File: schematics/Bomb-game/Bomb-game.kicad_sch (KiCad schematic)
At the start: 3 parts, among them U1 ADKeyboard

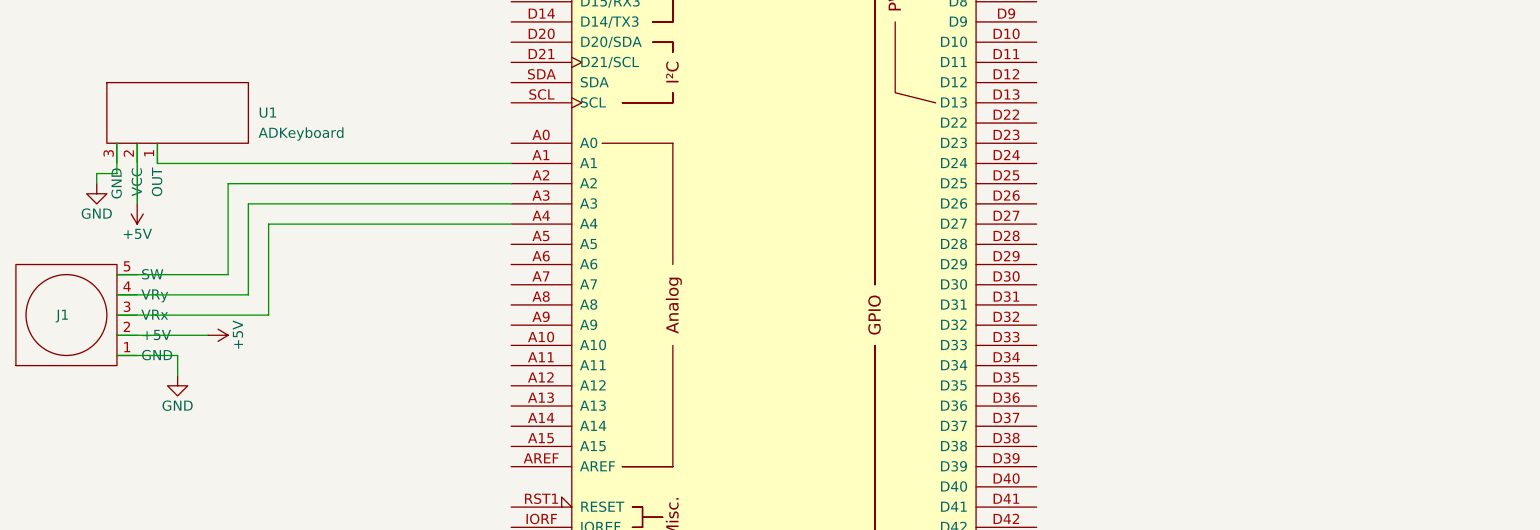
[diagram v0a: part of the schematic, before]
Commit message: Add relays to schematisc
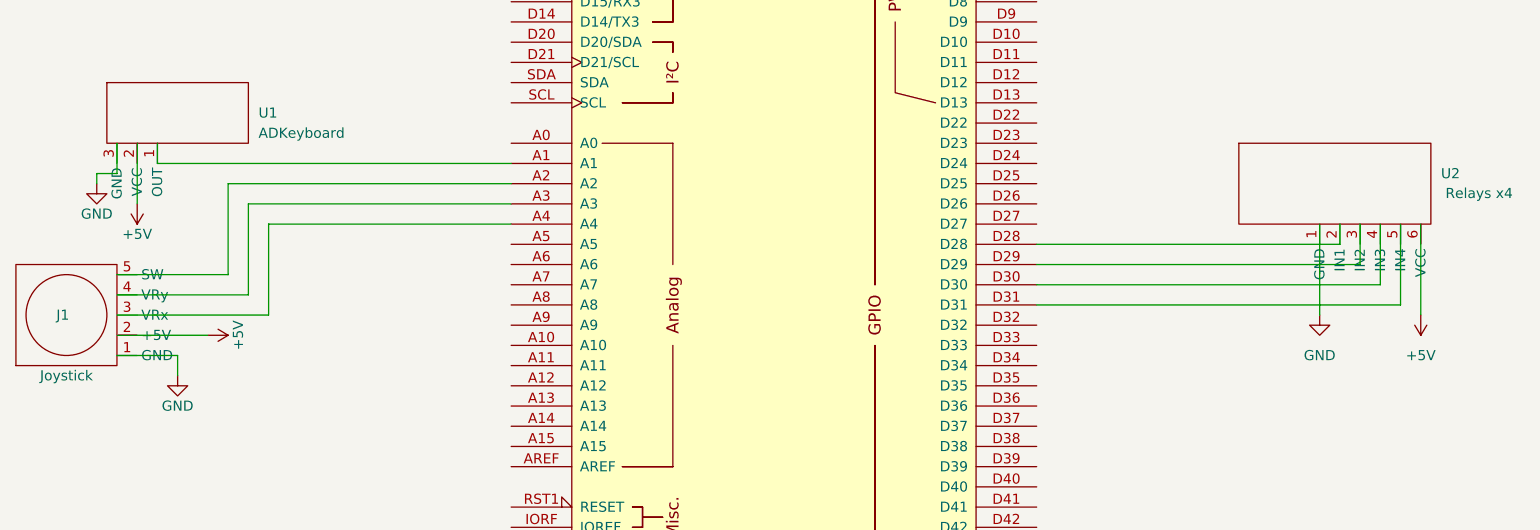
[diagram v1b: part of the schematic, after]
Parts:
- added U2: Relays x4, symbol Bomb-parts:Relay_x4
- J1: value ~ -> Joystick
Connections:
- net +5V: now also U2.6 (VCC)
- net GND: now also U2.1 (GND)
- net at XA1.D28: now also U2.2 (IN1)
- net at XA1.D29: now also U2.3 (IN2)
- net at XA1.D30: now also U2.4 (IN3)
- net at XA1.D31: now also U2.5 (IN4)
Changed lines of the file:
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@@
   (junction (at 109.22 138.43) (diameter 0) (color 0 0 0 0)
   )
+  (wire (pts (xy 220.98 72.39) (xy 220.98 82.55))
+    (stroke (width 0) (type default))
+  )
   (wire (pts (xy 73.66 78.74) (xy 73.66 67.31))
     (stroke (width 0) (type default))
@@
     (stroke (width 0) (type default))
   )
+  (wire (pts (xy 215.9 72.39) (xy 215.9 77.47))
+    (stroke (width 0) (type default))
+  )
   (wire (pts (xy 57.15 66.04) (xy 59.69 66.04))
     (stroke (width 0) (type default))
@@
     (stroke (width 0) (type default))
   )
+  (wire (pts (xy 210.82 72.39) (xy 210.82 83.82))
+    (stroke (width 0) (type default))
+  )
   (wire (pts (xy 109.22 123.19) (xy 105.41 123.19))
     (stroke (width 0) (type default))
@@
     (stroke (width 0) (type default))
   )
+  (wire (pts (xy 220.98 82.55) (xy 175.26 82.55))
+    (stroke (width 0) (type default))
+  )
   (wire (pts (xy 105.41 123.19) (xy 105.41 120.65))
     (stroke (width 0) (type default))
   )
+  (wire (pts (xy 223.52 72.39) (xy 223.52 83.82))
+    (stroke (width 0) (type default))
+  )
+  (wire (pts (xy 213.36 74.93) (xy 175.26 74.93))
+    (stroke (width 0) (type default))
+  )
   (wire (pts (xy 64.77 64.77) (xy 109.22 64.77))
     (stroke (width 0) (type default))
@@
     (stroke (width 0) (type default))
   )
+  (wire (pts (xy 215.9 77.47) (xy 175.26 77.47))
+    (stroke (width 0) (type default))
+  )
   (wire (pts (xy 105.41 118.11) (xy 109.22 118.11))
     (stroke (width 0) (type default))
@@
     (stroke (width 0) (type default))
   )
+  (wire (pts (xy 213.36 72.39) (xy 213.36 74.93))
+    (stroke (width 0) (type default))
+  )
   (wire (pts (xy 67.31 88.9) (xy 67.31 91.44))
     (stroke (width 0) (type default))
   )
+  (wire (pts (xy 218.44 80.01) (xy 175.26 80.01))
+    (stroke (width 0) (type default))
+  )
   (wire (pts (xy 59.69 86.36) (xy 71.12 86.36))
+    (stroke (width 0) (type default))
+  )
+  (wire (pts (xy 218.44 72.39) (xy 218.44 80.01))
     (stroke (width 0) (type default))
   )
@@
       (effects (font (size 1.27 1.27)) (justify right))
     )
-    (property "Value" "~" (at 55.88 86.36 0)
+    (property "Value" "Joystick" (at 53.34 91.44 90)
       (effects (font (size 1.27 1.27)))
     )
@@
         (path "/d5dfcc17-2f57-46e4-9b81-9957aca5a4a9"
           (reference "#PWR01") (unit 1)
+        )
+      )
+    )
+  )
+  (symbol (lib_id "Bomb-parts:Relay_x4") (at 214.63 68.58 0) (unit 1)
+    (in_bom yes) (on_board yes) (dnp no)
+    (property "Reference" "U2" (at 226.06 66.04 0)
+      (effects (font (size 1.27 1.27)) (justify left))
+    )
+    (property "Value" "Relays x4" (at 230.8513 68.5236 0)
+      (effects (font (size 1.27 1.27)))
+    )
+    (property "Footprint" "" (at 214.63 68.58 0)
+      (effects (font (size 1.27 1.27)) hide)
+    )
+    (property "Datasheet" "" (at 214.63 68.58 0)
+      (effects (font (size 1.27 1.27)) hide)
+    )
+    (pin "1")
+    (pin "2")
+    (pin "3")
+    (pin "4")
+    (pin "5")
+    (pin "6")
+    (instances
+      (project "Bomb-game"
+        (path "/d5dfcc17-2f57-46e4-9b81-9957aca5a4a9"
+          (reference "U2") (unit 1)
         )
       )
@@
         )
       )
+    )
+  )
+  (symbol (lib_id "power:GND") (at 210.82 83.82 0) (unit 1)
+    (in_bom yes) (on_board yes) (dnp no) (fields_autoplaced)
+    (property "Reference" "#PWR08" (at 210.82 90.17 0)
+      (effects (font (size 1.27 1.27)) hide)
+    )
+    (property "Value" "GND" (at 210.82 88.9 0)
+      (effects (font (size 1.27 1.27)))
+    )
+    (property "Footprint" "" (at 210.82 83.82 0)
+      (effects (font (size 1.27 1.27)) hide)
+    )
+    (property "Datasheet" "" (at 210.82 83.82 0)
+      (effects (font (size 1.27 1.27)) hide)
+    )
+    (pin "1")
+    (instances
+      (project "Bomb-game"
+        (path "/d5dfcc17-2f57-46e4-9b81-9957aca5a4a9"
+          (reference "#PWR08") (unit 1)
+        )
+      )
+    )
+  )
+  (symbol (lib_id "power:+5V") (at 223.52 83.82 180) (unit 1)
+    (in_bom yes) (on_board yes) (dnp no) (fields_autoplaced)
+    (property "Reference" "#PWR09" (at 223.52 80.01 0)
+      (effects (font (size 1.27 1.27)) hide)
+    )
+    (property "Value" "+5V" (at 223.52 88.9 0)
+      (effects (font (size 1.27 1.27)))
+    )
+    (property "Footprint" "" (at 223.52 83.82 0)
+      (effects (font (size 1.27 1.27)) hide)
+    )
+    (property "Datasheet" "" (at 223.52 83.82 0)
+      (effects (font (size 1.27 1.27)) hide)
+    )
+    (pin "1")
+    (instances
+      (project "Bomb-game"
+        (path "/d5dfcc17-2f57-46e4-9b81-9957aca5a4a9"
+          (reference "#PWR09") (unit 1)
+        )
+      )

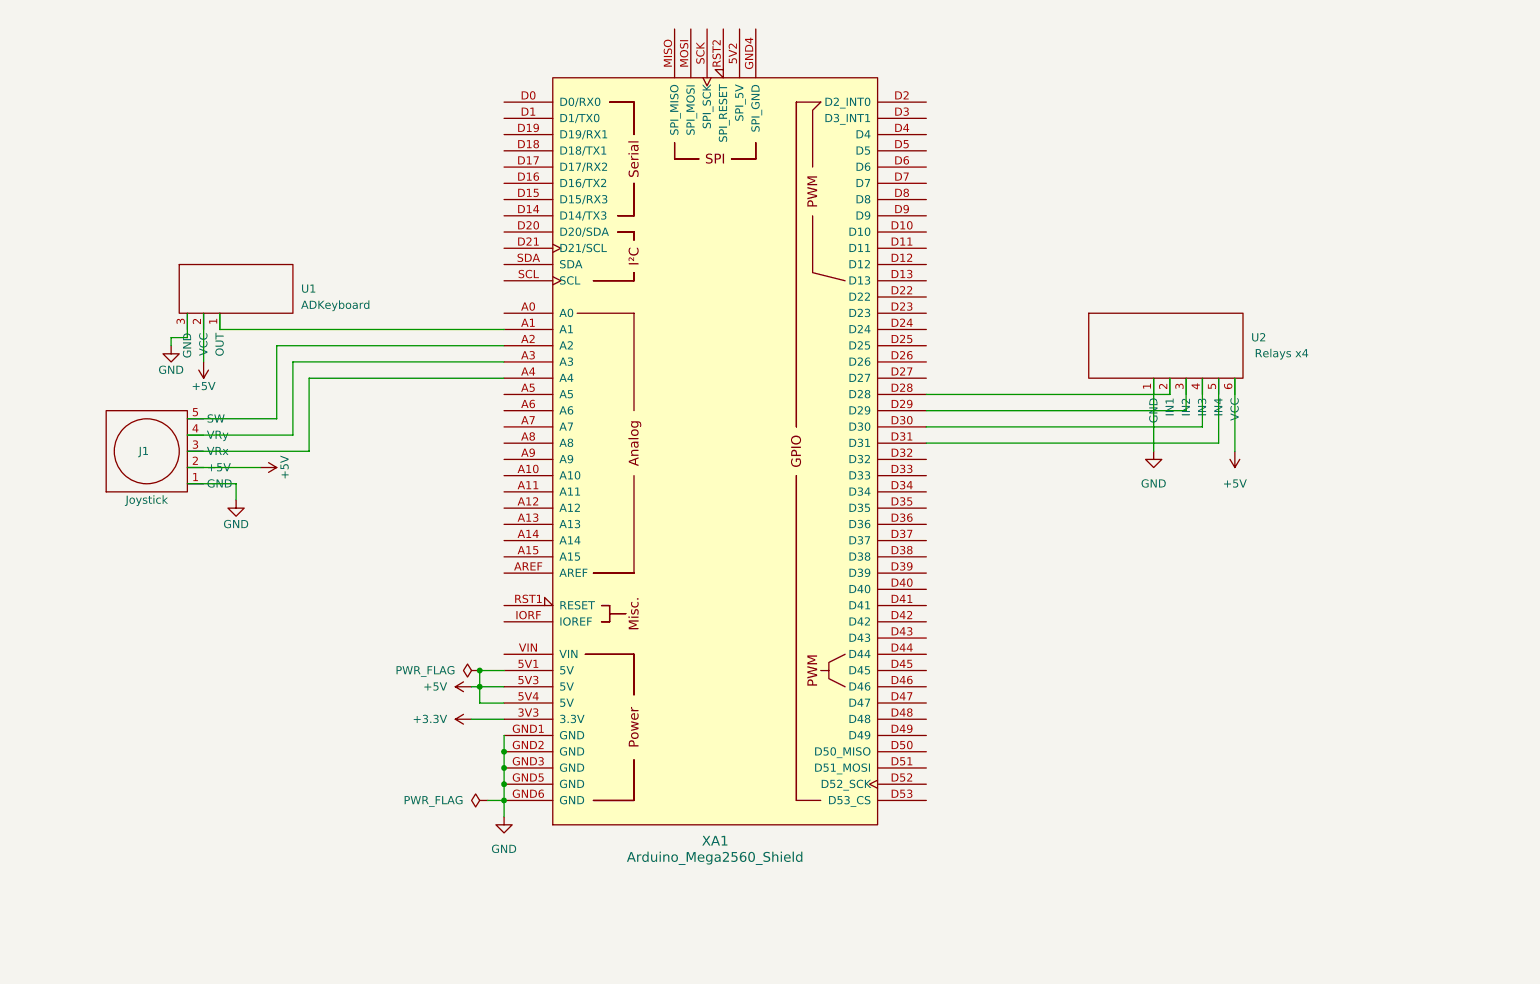
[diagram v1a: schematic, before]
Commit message: Update schematics, add emergency button
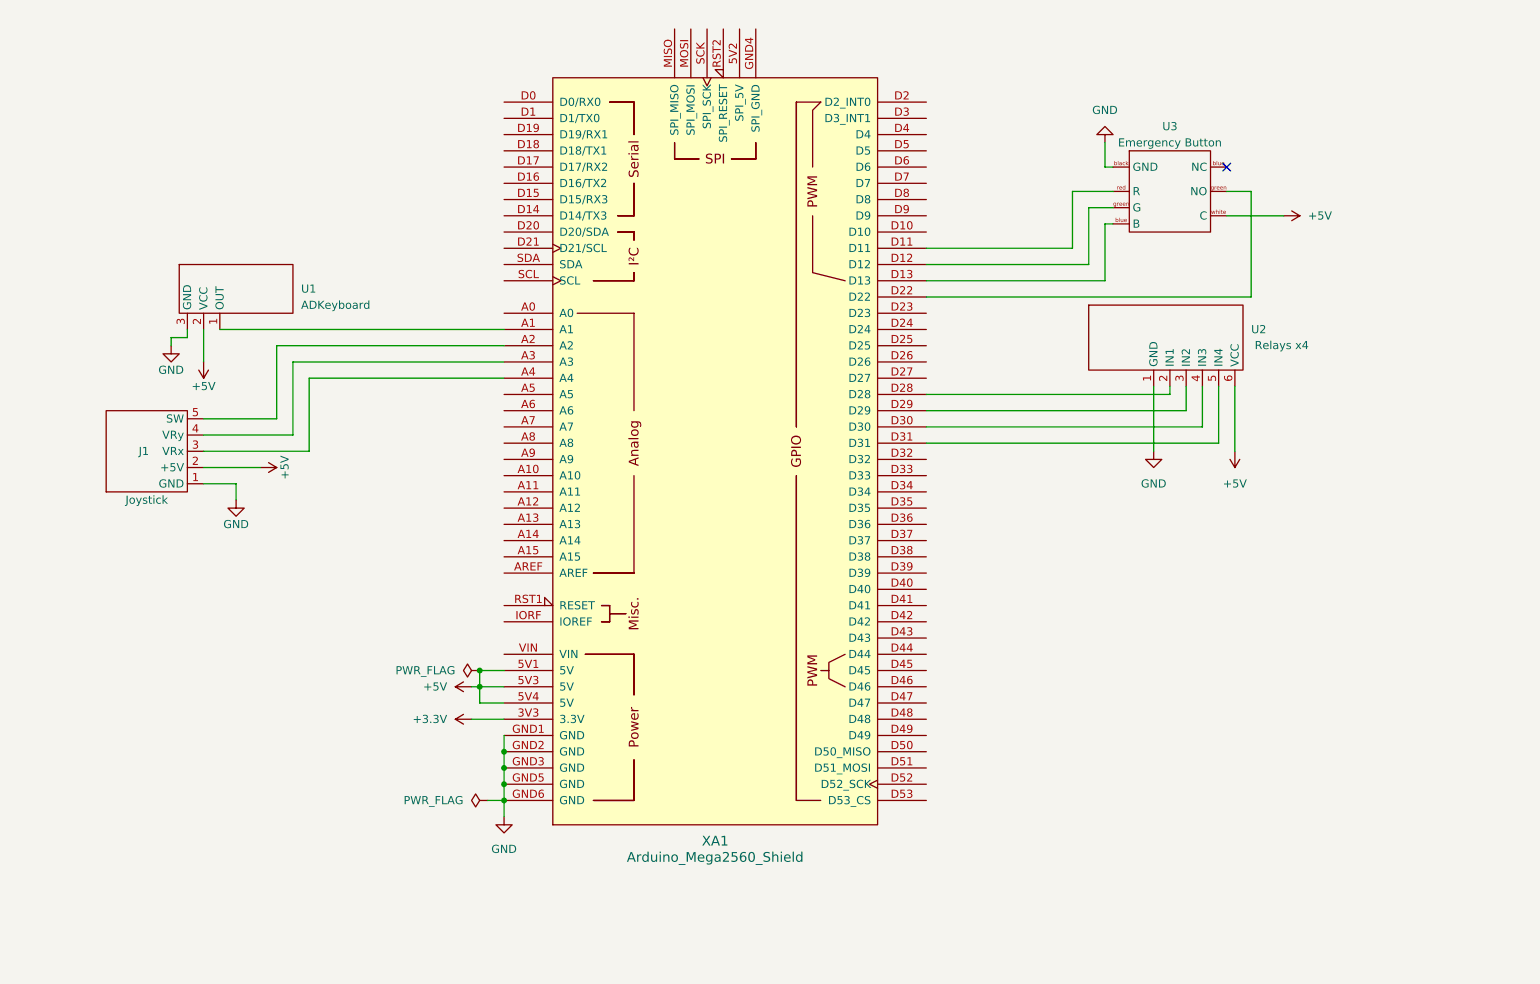
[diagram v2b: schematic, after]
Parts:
- added U3: Emergency Button, symbol Bomb-parts:Emergency_button
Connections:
- net +5V: now also U3.white (C)
- net GND: now also U3.black (GND)
- net at XA1.D11: now also U3.red (R)
- net at XA1.D12: now also U3.green (NO)
- net at XA1.D13: now also U3.blue (NC)
- net at XA1.D22: now also U3.green (NO)
- no-connect marks 0 -> 1
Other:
- moved on the sheet: U1, U2

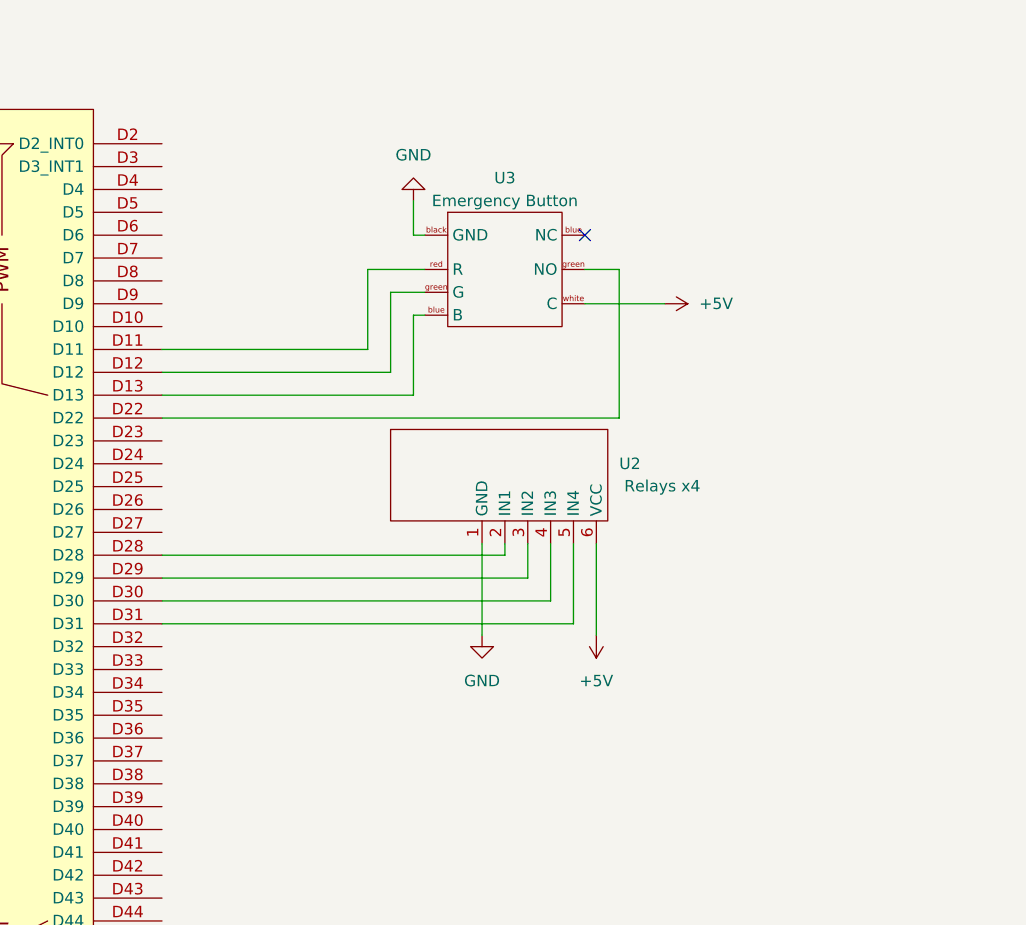
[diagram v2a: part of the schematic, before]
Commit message: Update schematics with 8x8 WS2812B
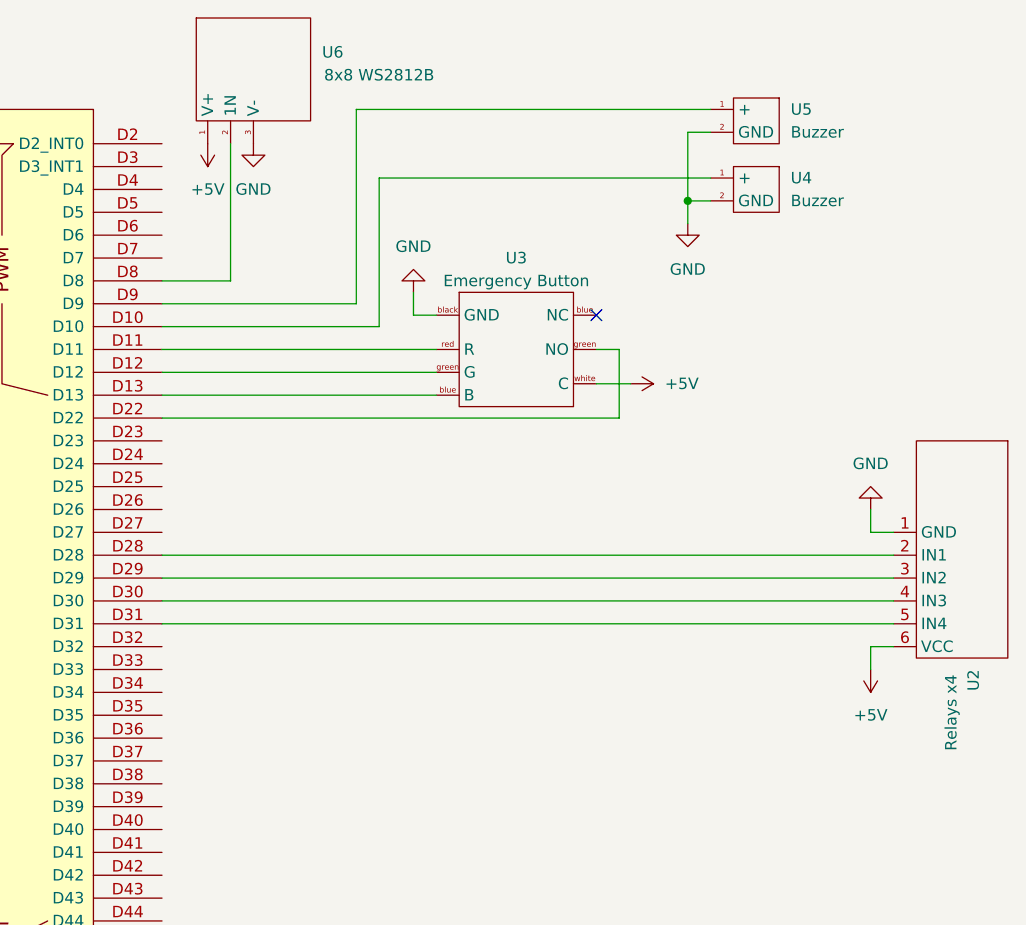
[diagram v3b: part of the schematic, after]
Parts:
- added U4, U5: Buzzer, symbol Bomb-parts:Buzzer
- added U6: 8x8 WS2812B, symbol Bomb-parts:WS2812B_8x8
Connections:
- net +5V: now also U6.1 (V+)
- net GND: now also U4.2 (GND), U5.2 (GND), U6.3 (V-)
- net at XA1.D10: now also U4.1 (+)
- net at XA1.D8: now also U6.2 (1N)
- net at XA1.D9: now also U5.1 (+)
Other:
- moved on the sheet: U2, U3

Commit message: Save schematics :)
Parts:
- added U7: LCD 1602, symbol Bomb-parts:LCD_1602
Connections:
- net +5V: now also U7.2 (VCC)
- net GND: now also U7.1 (GND)
- net at XA1.D20 (D20/SDA): now also U7.3 (SDA)
- net at XA1.D21 (D21/SCL): now also U7.4 (SCL)
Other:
- moved on the sheet: J1, U1, U2, U3, U4, U5, U6, XA1
